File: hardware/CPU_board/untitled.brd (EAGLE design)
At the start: 128.9 x 94.9 mm, 52 parts, among them IC1 MAX232ECWE, IC2 MAX232ECWE, IC3 AM29F040J, IC4 74HCT138D, IC5 LM2596S, J2 POWER_JACKSLT, U1 AS6C4008-55SIN, Y1 CRYSTAL-GROUNDEDSMD-5X3.2

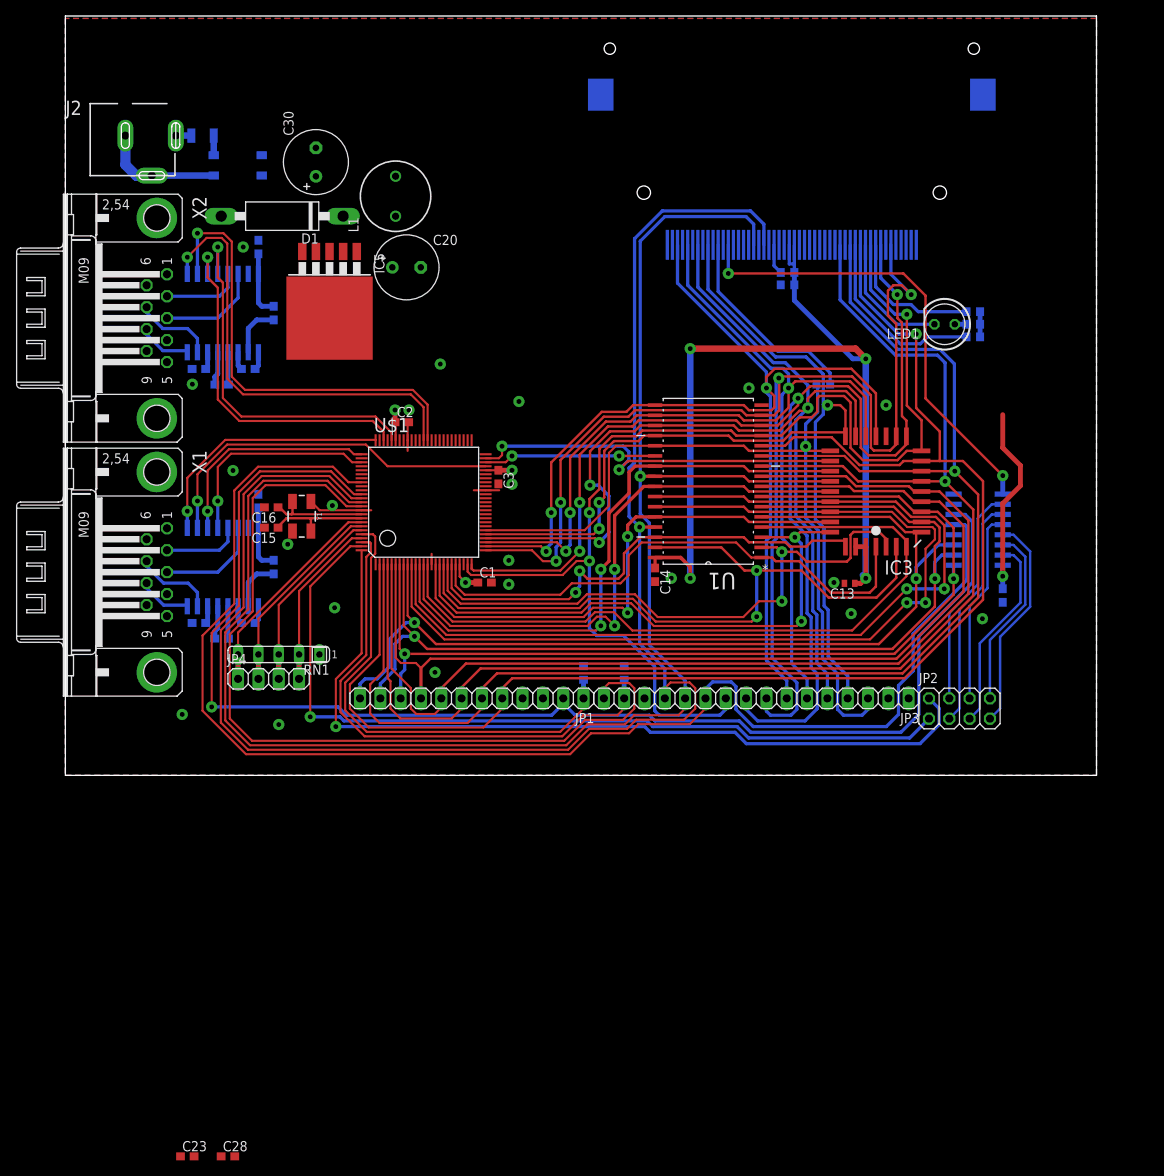
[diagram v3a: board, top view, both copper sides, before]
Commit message: Pullup resistors added
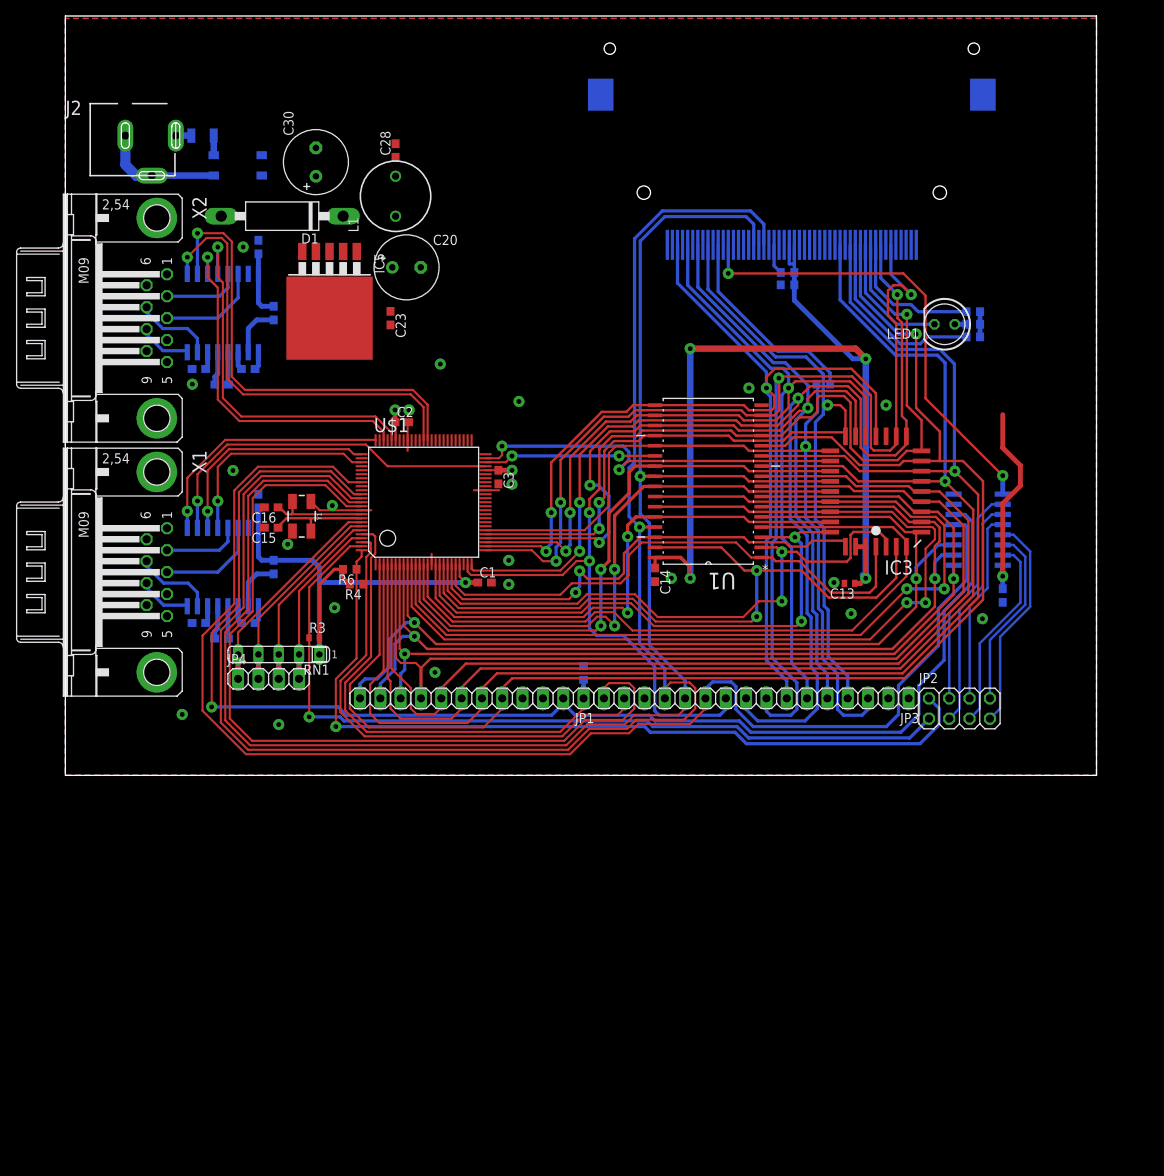
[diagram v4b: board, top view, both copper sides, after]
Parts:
- added R3: (no value), rcl:R0402
- added R6: (no value), rcl:R0603
- moved C28 127.5 mm to (41.3, 77.5), turned to 90 degrees
- moved C23 107.8 mm to (40.6, 56.5), turned to 270 degrees
- moved R4 35.2 mm to (36.4, 23.3), flipped to the top, turned to 180 degrees
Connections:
- net !IRQ1: now also R3.1
- net !IRQ2: now also R6.1
- net 5V: now also R3.2, R6.2
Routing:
- net 5V: track 171.3 -> 221.3 mm
- net !INT: track 65.6 -> 63.8 mm

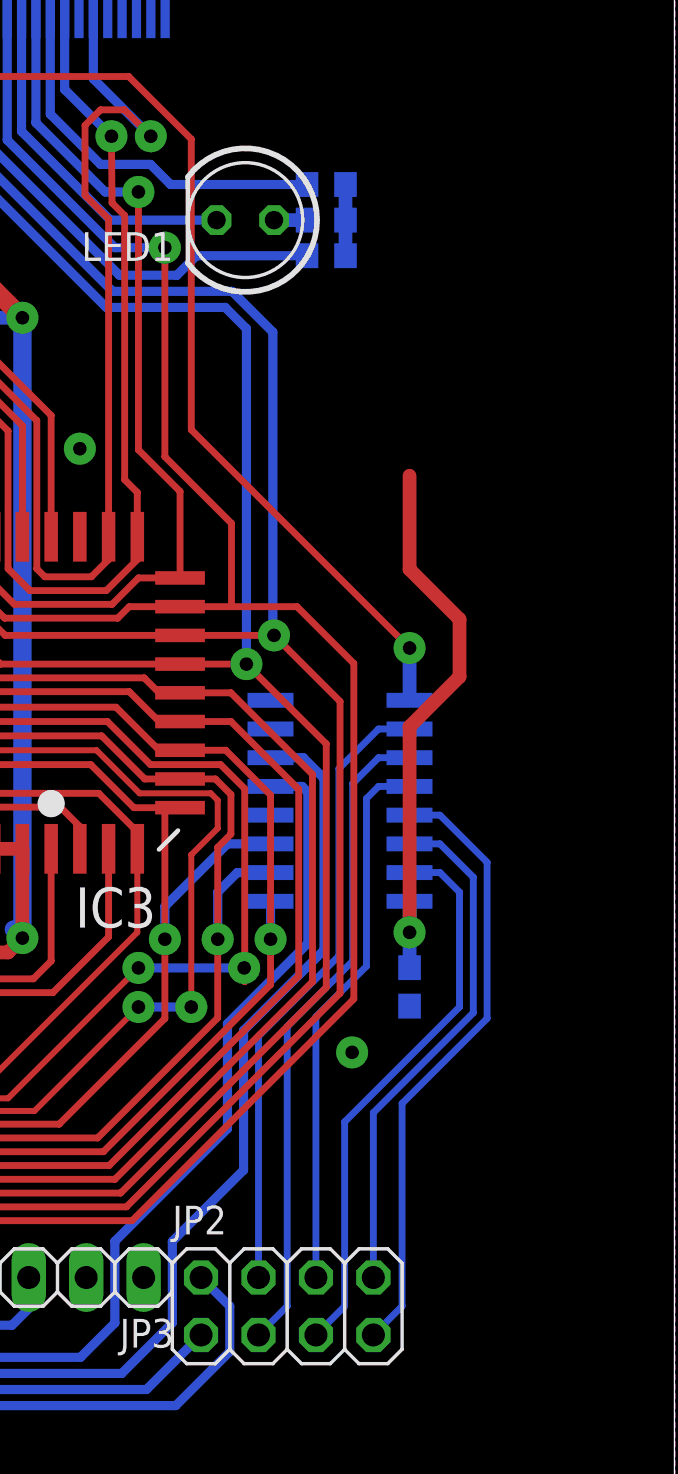
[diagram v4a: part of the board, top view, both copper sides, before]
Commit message: I/O address decoder adjusted to internal registers of Z80182
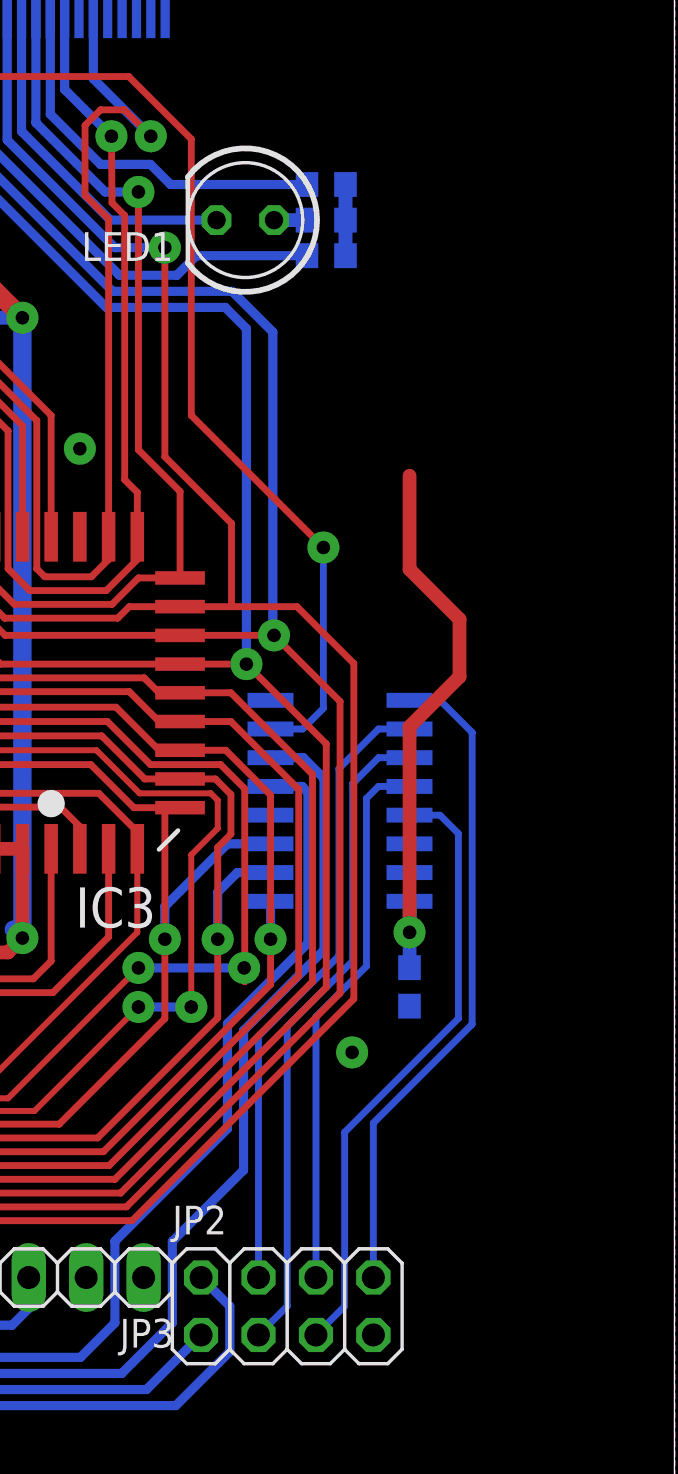
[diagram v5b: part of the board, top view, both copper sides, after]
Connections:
- removed net CS0: IC4.15, JP2.5
- removed net CS1: IC4.14, JP2.8
- removed net CS7: IC4.7
- new net CF6: IC4.9, JP2.8
- new net CS0_NO_USE: IC4.15
- new net CS1_NO_USE: IC4.14
- net CF_CS0: now also IC4.7; no longer IC4.9
- net CS2: now also JP2.5; no longer JP2.7
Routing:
- net CF6: track 0.00 -> 29.3 mm
- net CS0: track 24.8 -> 0.00 mm
- net CS1: track 23.0 -> 0.00 mm
- net CF_CS0: track 58.2 -> 59.7 mm
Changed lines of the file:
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@@
 <signal name="CF_CS0">
 <contactref element="CON1" pad="7"/>
-<contactref element="IC4" pad="9"/>
 <wire x1="82.8675" y1="65.675" x2="82.8675" y2="62.103" width="0.4064" layer="16"/>
 <via x="82.8675" y="62.103" extent="1-16" drill="0.6" diameter="1.4224" shape="octagon"/>
 <wire x1="82.8675" y1="62.103" x2="104.7496" y2="62.103" width="0.3048" layer="1"/>
-<via x="117.1702" y="36.83" extent="1-16" drill="0.6" diameter="1.4224" shape="octagon"/>
-<wire x1="117.1702" y1="34.5186" x2="117.1702" y2="36.83" width="0.6096" layer="16"/>
-<wire x1="107.5182" y1="46.482" x2="117.1702" y2="36.83" width="0.3048" layer="1"/>
-<wire x1="107.5182" y1="59.3344" x2="107.5182" y2="46.482" width="0.3048" layer="1"/>
+<via x="113.3602" y="41.275" extent="1-16" drill="0.6" diameter="1.4224" shape="octagon"/>
+<wire x1="107.5182" y1="47.117" x2="113.3602" y2="41.275" width="0.3048" layer="1"/>
+<wire x1="107.5182" y1="59.3344" x2="107.5182" y2="47.117" width="0.3048" layer="1"/>
 <wire x1="104.7496" y1="62.103" x2="107.5182" y2="59.3344" width="0.3048" layer="1"/>
+<contactref element="IC4" pad="7"/>
+<wire x1="113.3602" y1="41.275" x2="113.3602" y2="34.163" width="0.3048" layer="16"/>
+<wire x1="113.3602" y1="34.163" x2="112.4458" y2="33.2486" width="0.3048" layer="16"/>
+<wire x1="112.4458" y1="33.2486" x2="111.0234" y2="33.2486" width="0.3048" layer="16"/>
 </signal>
 <signal name="N$31">
@@
 <wire x1="89.0778" y1="52.3748" x2="92.8878" y2="52.3748" width="0.4064" layer="16"/>
 </signal>
-<signal name="CS0">
+<signal name="CS0_NO_USE">
 <contactref element="IC4" pad="15"/>
-<wire x1="113.03" y1="6.4516" x2="114.3" y2="7.7216" width="0.3048" layer="16"/>
-<wire x1="114.3" y1="7.7216" x2="114.3" y2="15.875" width="0.3048" layer="16"/>
-<wire x1="114.3" y1="15.875" x2="119.38" y2="20.955" width="0.3048" layer="16"/>
-<wire x1="119.38" y1="20.955" x2="119.38" y2="26.035" width="0.3048" layer="16"/>
-<wire x1="119.38" y1="26.035" x2="118.5164" y2="26.8986" width="0.3048" layer="16"/>
-<wire x1="117.1702" y1="26.8986" x2="118.5164" y2="26.8986" width="0.3048" layer="16"/>
-<contactref element="JP2" pad="5"/>
 </signal>
-<signal name="CS1">
+<signal name="CS1_NO_USE">
 <contactref element="IC4" pad="14"/>
-<wire x1="115.57" y1="8.9916" x2="115.57" y2="16.2814" width="0.3048" layer="16"/>
-<wire x1="115.57" y1="16.2814" x2="119.9896" y2="20.701" width="0.3048" layer="16"/>
-<wire x1="119.9896" y1="20.701" x2="119.9896" y2="26.6954" width="0.3048" layer="16"/>
-<wire x1="119.9896" y1="26.6954" x2="118.5164" y2="28.1686" width="0.3048" layer="16"/>
-<wire x1="117.1702" y1="28.1686" x2="118.5164" y2="28.1686" width="0.3048" layer="16"/>
-<contactref element="JP2" pad="8"/>
 </signal>
 <signal name="CS2">
 <contactref element="IC4" pad="13"/>
-<wire x1="115.57" y1="6.4516" x2="116.84" y2="7.7216" width="0.3048" layer="16"/>
-<wire x1="116.84" y1="7.7216" x2="116.84" y2="16.6878" width="0.3048" layer="16"/>
-<wire x1="116.84" y1="16.6878" x2="120.5992" y2="20.447" width="0.3048" layer="16"/>
-<wire x1="120.5992" y1="20.447" x2="120.5992" y2="27.3558" width="0.3048" layer="16"/>
-<wire x1="120.5992" y1="27.3558" x2="118.5164" y2="29.4386" width="0.3048" layer="16"/>
+<wire x1="114.3" y1="7.7216" x2="114.3" y2="15.4178" width="0.3048" layer="16"/>
+<wire x1="114.3" y1="15.4178" x2="119.3292" y2="20.447" width="0.3048" layer="16"/>
+<wire x1="119.3292" y1="20.447" x2="119.3292" y2="28.6258" width="0.3048" layer="16"/>
+<wire x1="119.3292" y1="28.6258" x2="118.5164" y2="29.4386" width="0.3048" layer="16"/>
 <wire x1="117.1702" y1="29.4386" x2="118.5164" y2="29.4386" width="0.3048" layer="16"/>
-<contactref element="JP2" pad="7"/>
+<contactref element="JP2" pad="5"/>
+<wire x1="114.3" y1="7.7216" x2="113.03" y2="6.4516" width="0.3048" layer="16"/>
 </signal>
 <signal name="CS3">
@@
 <contactref element="JP2" pad="4"/>
 </signal>
-<signal name="CS7">
-<contactref element="IC4" pad="7"/>
-</signal>
 <signal name="!BUSACK">
 <contactref element="U$1" pad="94"/>
@@
 <wire x1="26.67" y1="20.6756" x2="26.67" y2="14.478" width="0.2667" layer="1"/>
 </signal>
+<signal name="CF6">
+<contactref element="IC4" pad="9"/>
+<contactref element="JP2" pad="8"/>
+<wire x1="119.9388" y1="20.193" x2="115.57" y2="15.8242" width="0.3048" layer="16"/>
+<wire x1="115.57" y1="15.8242" x2="115.57" y2="8.9916" width="0.3048" layer="16"/>
+<wire x1="118.5164" y1="34.5186" x2="117.1702" y2="34.5186" width="0.3048" layer="16"/>
+<wire x1="119.9388" y1="20.193" x2="119.9388" y2="33.0962" width="0.3048" layer="16"/>
+<wire x1="119.9388" y1="33.0962" x2="118.5164" y2="34.5186" width="0.3048" layer="16"/>
+</signal>
 </signals>

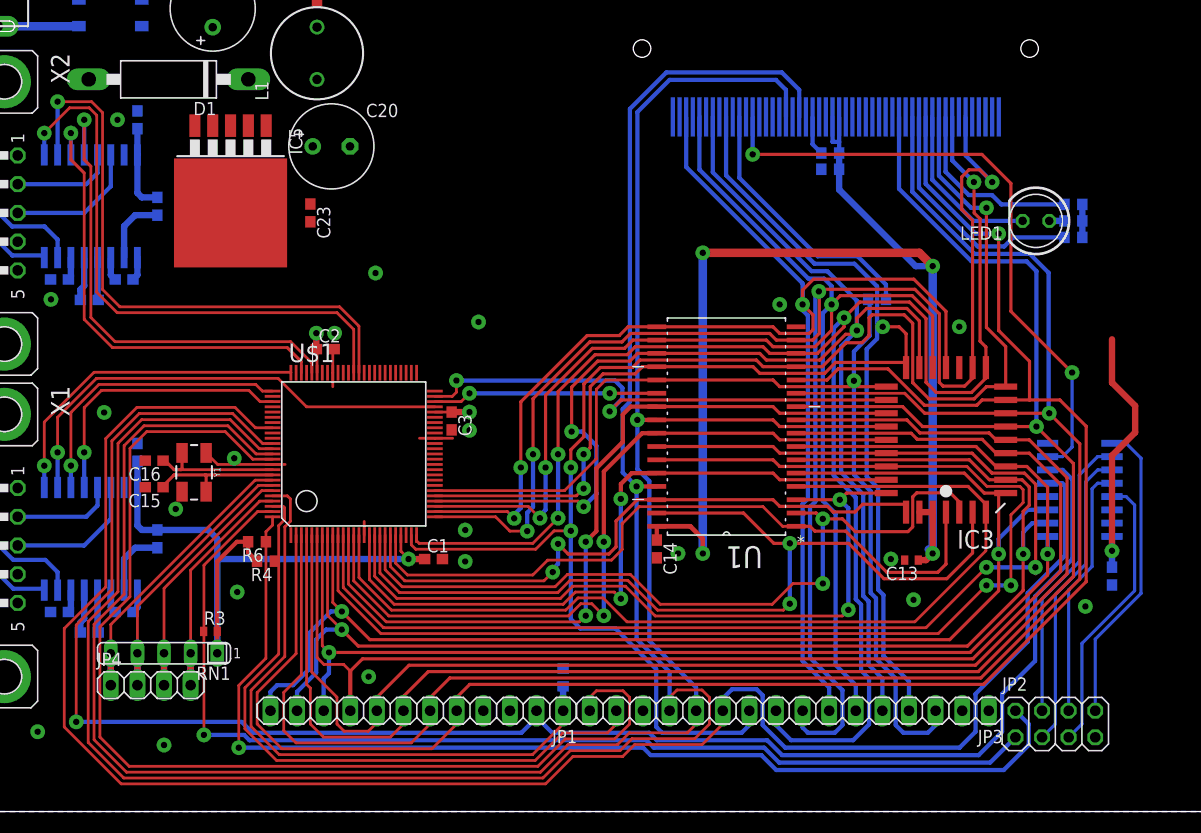
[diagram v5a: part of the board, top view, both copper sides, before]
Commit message: Reset supervisor added, GND tracing changed
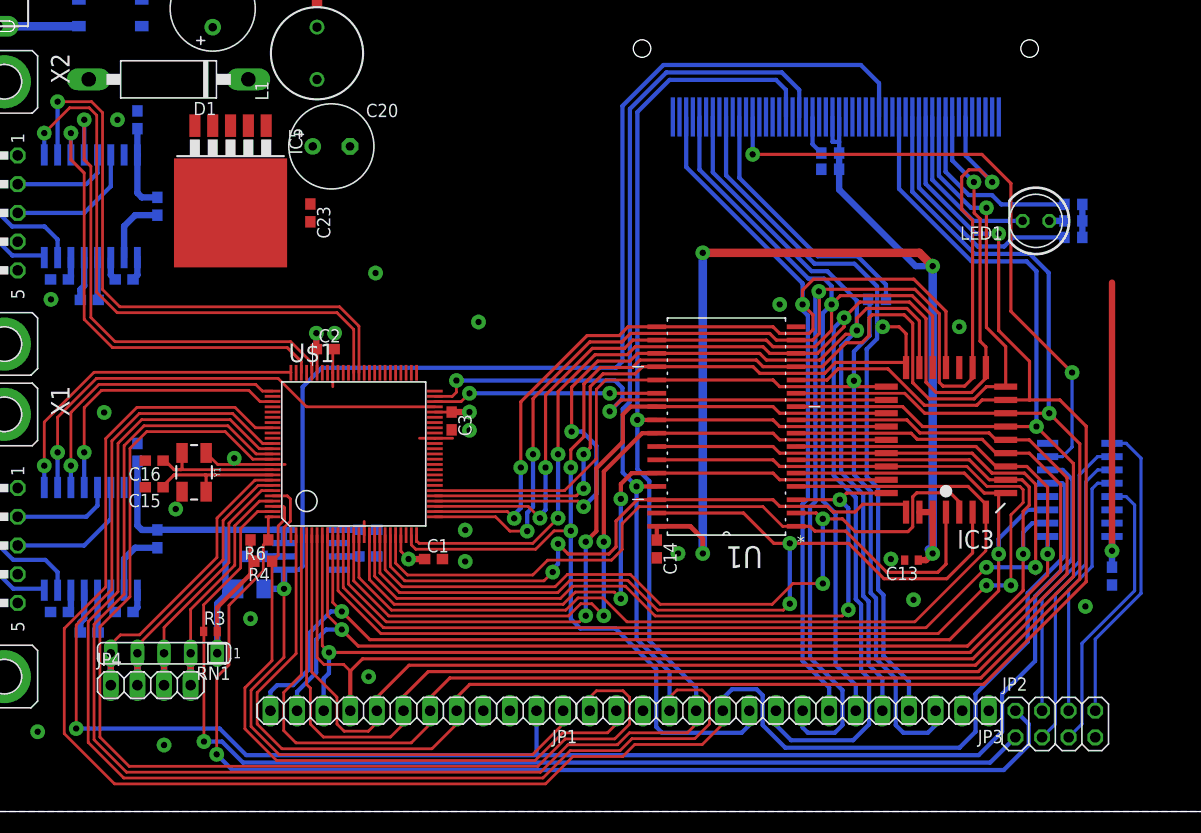
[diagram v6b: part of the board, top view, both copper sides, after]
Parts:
- added C18, C19: (no value), rcl:C0603
- added R9: (no value), rcl:R0603
- added U$2: TL7705, mw:SOIC8
- R5: device rcl:R0603 -> rcl:R1206
- moved R5 31.1 mm to (34.9, 20.6), turned to 0 degrees
- moved R6 0.29 mm to (35.8, 25.3)
- moved R4 0.25 mm to (36.1, 23.3)
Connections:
- removed net !RESET: CON1.41
- new net N$35: R9.2, U$2.6
- new net N$36: C18.1, U$2.3
- new net N$37: C19.1, U$2.1
- net !RST: now also CON1.41, U$2.5
- net 5V: now also U$2.7, U$2.8
- net GND: now also C18.2, C19.2, R9.1, U$2.4
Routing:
- net !RST: track 60.8 -> 167.2 mm, vias 0 -> 1
- net 5V: track 221.3 -> 213.9 mm, vias 8 -> 9
- net !IRQ2: track 104.7 -> 108.1 mm
- net !M1: track 168.0 -> 170.7 mm
- net N$35: track 0.00 -> 2.04 mm
- net N$37: track 0.00 -> 1.96 mm
- net N$36: track 0.00 -> 1.96 mm
- net !WAIT: track 30.0 -> 31.1 mm

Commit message: Reset circuit updated
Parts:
- added JP5: (no value), pinhead:1X02
- added R10: (no value), rcl:R0603
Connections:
- new net N$38: JP5.2, R10.1, U$2.2
- net 5V: now also R10.2
- net GND: now also JP5.1
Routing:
- net N$38: track 0.00 -> 15.1 mm
- net !INT: track 63.3 -> 64.3 mm
- net GND: vias 21 -> 20
